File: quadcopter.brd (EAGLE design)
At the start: 130 x 130 mm, 66 parts, among them J1 ISP, J4 SIP-10_TH-254X10, M1 MOTOR_PADS, M2 MOTOR_PADS, M3 MOTOR_PADS, M4 MOTOR_PADS, U1 ATMEGA128RFA1, Y1 16MHz

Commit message: Version before generating cam
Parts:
- LED2, LED3: value BLUE -> green; device Yueqi Wang-Lab2:LED5MM -> quadparts_prebuilt:LEDSC125X200X120-2_HS
- moved LED4 73.5 mm to (31.0, -3.00), turned to 0 degrees
- moved LED1 73.5 mm to (31.0, 3.00), turned to 0 degrees
- moved C16 68.3 mm to (6.74, 37.6), turned to 270 degrees
- moved R15 48.0 mm to (-19.1, -15.2), turned to 270 degrees
- moved U$7 46.2 mm to (-7.45, -21.6), turned to 0 degrees
- moved C19 35.8 mm to (22.6, -16.8), turned to 270 degrees
- moved C24 35.1 mm to (-6.99, 4.57)
- moved U$2 33.2 mm to (17.0, -22.0), turned to 270 degrees
- moved C23 26.2 mm to (8.12, 4.38), turned to 180 degrees
- moved BATT1 24.8 mm to (0.00, 0.00), turned to 180 degrees
- moved C18 22.1 mm to (11.8, -16.2), turned to 90 degrees
- moved J2 22.0 mm to (1.28, -22.2), turned to 270 degrees
- moved C22 20.1 mm to (8.15, 7.99), turned to 180 degrees
- moved C20 15.7 mm to (0.83, 7.28), turned to 90 degrees
- moved MOFSET4 15.4 mm to (30.5, -26.6)
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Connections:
- net GND: now also LED2.C, LED3.C; no longer LED2.K, LED3.K
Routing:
- net DTR: track 86.9 -> 8.24 mm, vias 2 -> 0
- net VBAT: track 127.0 -> 84.4 mm, vias 4 -> 6
- net BAT_GND: track 234.5 -> 275.4 mm, vias 2 -> 0
- net PG1: track 22.1 -> 60.4 mm, vias 0 -> 2
- net SCK: track 21.9 -> 59.8 mm
- net PG0: track 27.1 -> 64.2 mm
- net RX0: track 47.8 -> 82.5 mm
- net RESET: track 102.6 -> 68.2 mm, vias 2 -> 1
- net MOSI: track 27.9 -> 62.1 mm
- net GND: track 266.6 -> 297.4 mm, vias 45 -> 41
- net PE3: track 124.3 -> 99.1 mm
- net SDA: track 114.8 -> 89.9 mm, vias 5 -> 2
- net TX0: track 47.7 -> 62.7 mm
- net FILTERED_1: track 19.8 -> 34.3 mm, vias 0 -> 2
- net PB5: track 111.1 -> 97.4 mm, vias 0 -> 1
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- added copper zone on layer 1, net GND
- added copper zone on layer 2, net GND
- added copper zone on layer 2, net N$3
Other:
- board text added: "CTS"
- board text added: "DTR"
- board text added: "RXI"
- board text added: "TXO"

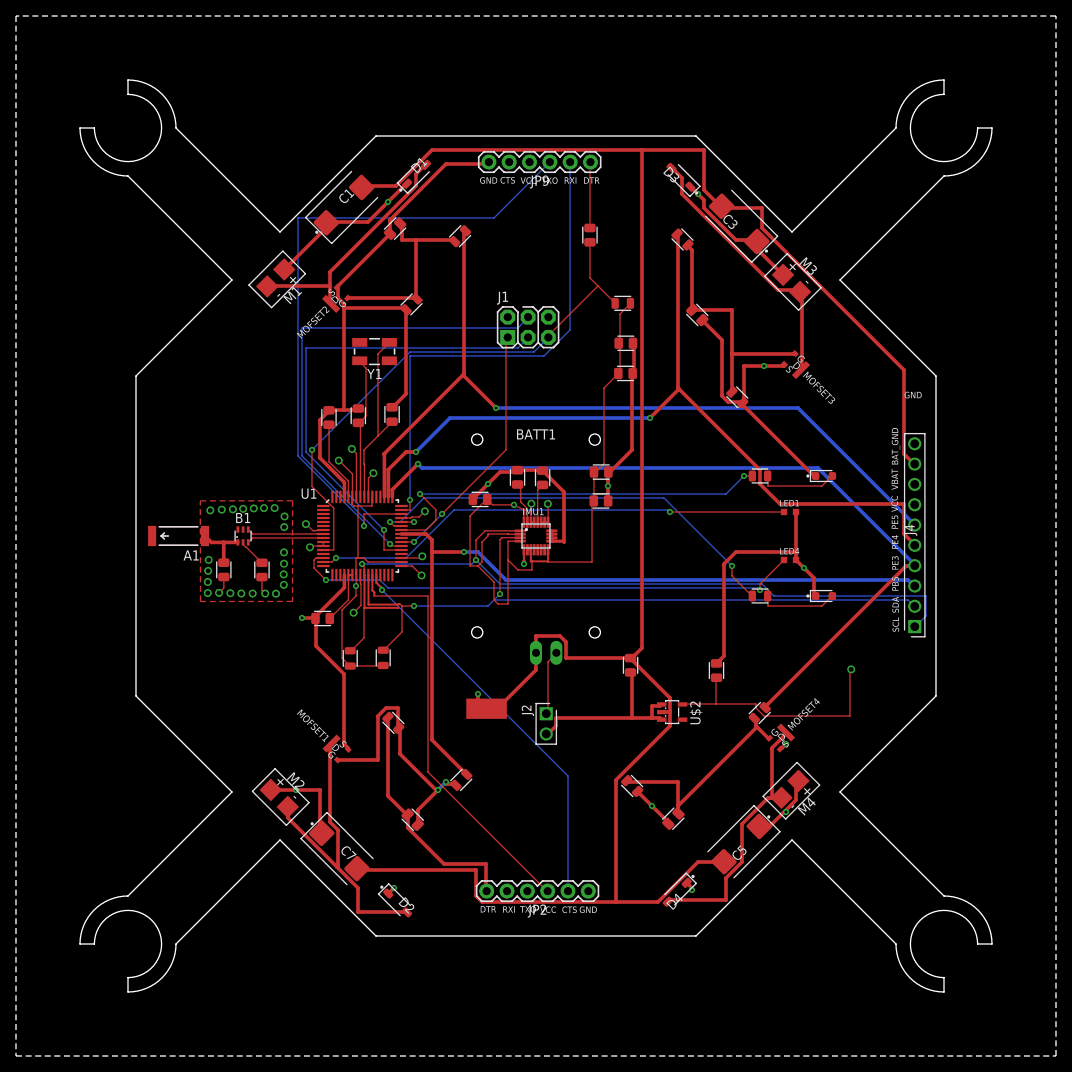
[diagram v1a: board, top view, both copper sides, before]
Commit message: Version May 8th 11pm
Version before rerun the autorouter with new dru
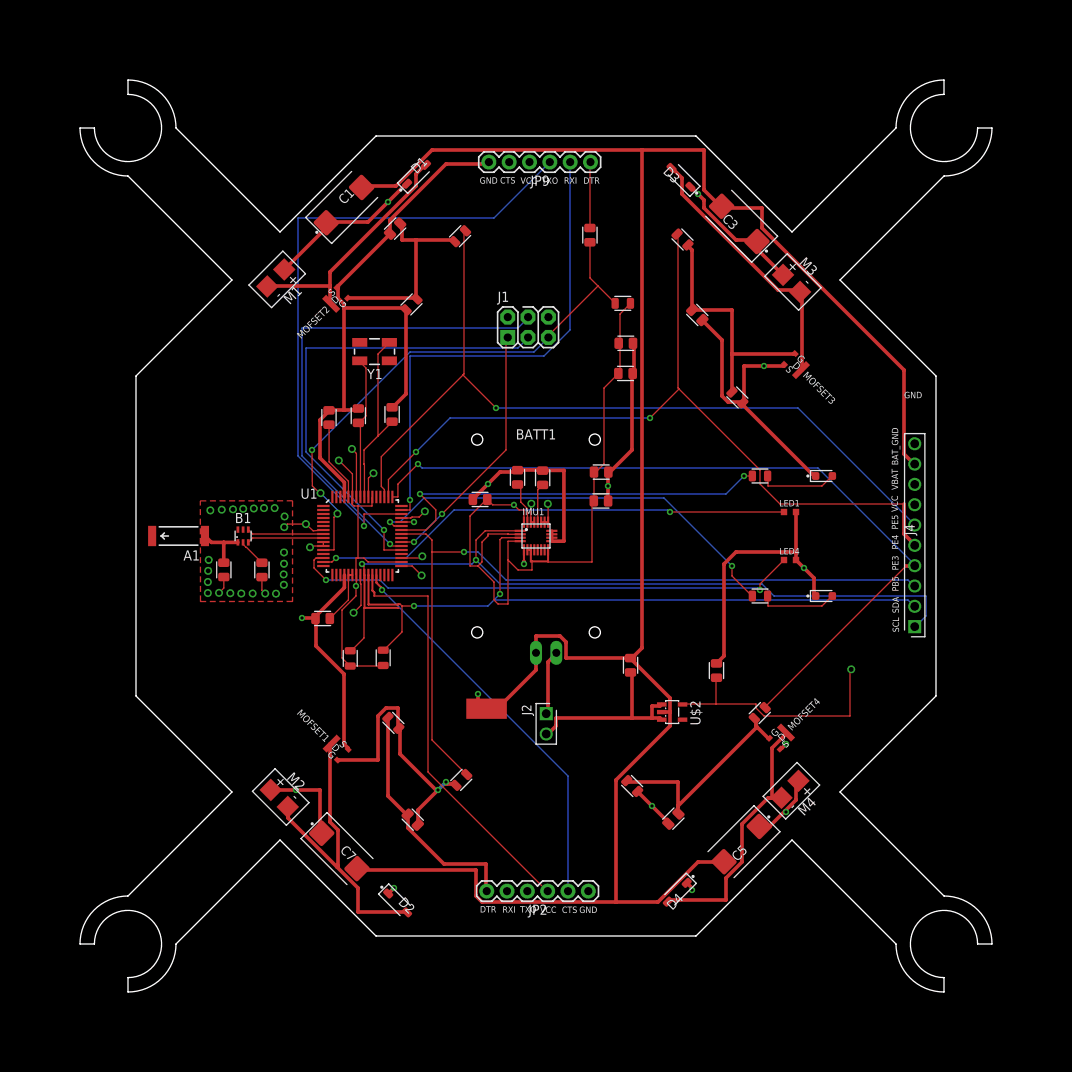
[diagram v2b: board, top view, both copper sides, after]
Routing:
- net GND: track 297.4 -> 301.6 mm
- net PE4: track 104.3 -> 103.4 mm
- net RESET: track 68.2 -> 68.7 mm, vias 1 -> 3
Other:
- board size 130 x 130 mm -> 114 x 114 mm

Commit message: Board and Schematic that pass DFM
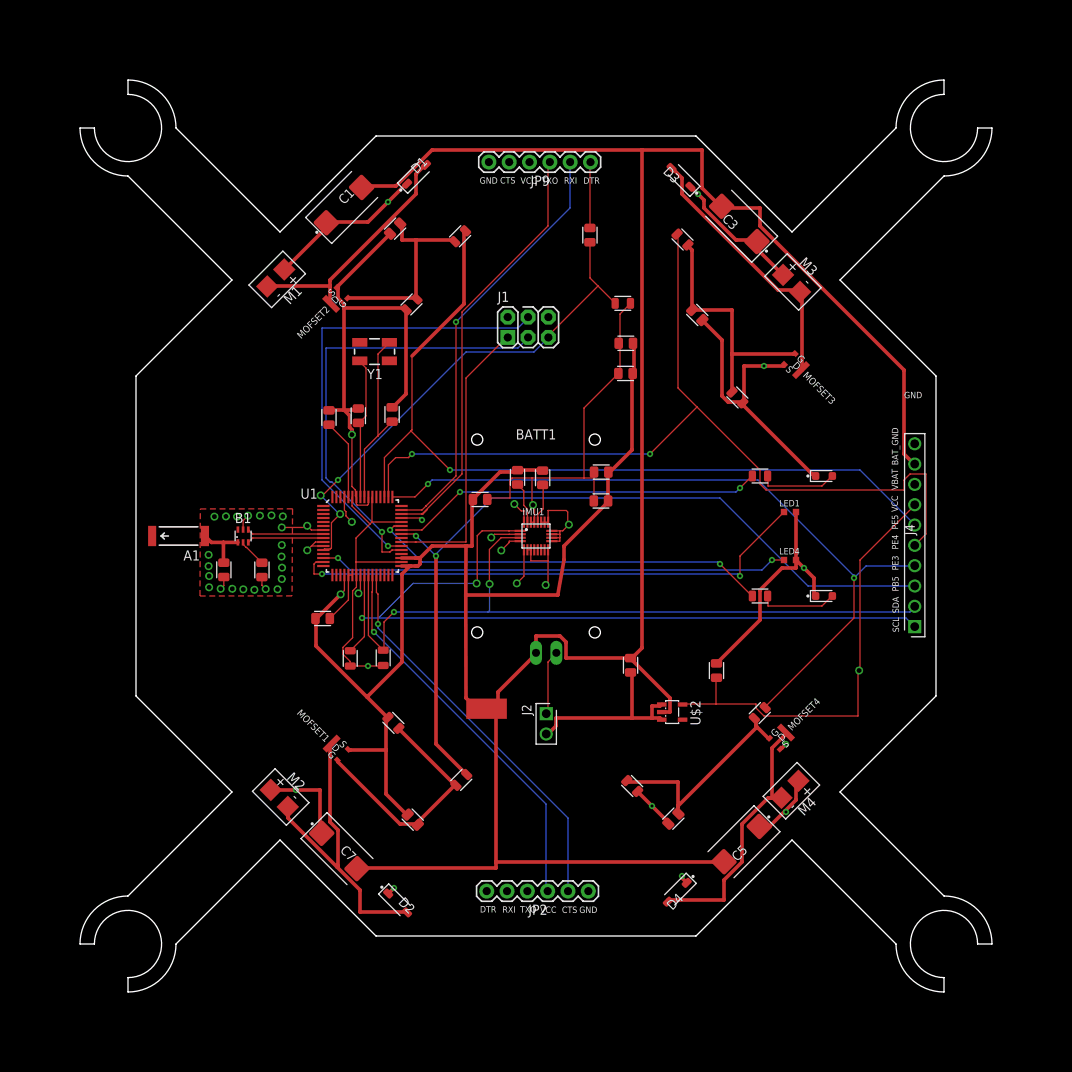
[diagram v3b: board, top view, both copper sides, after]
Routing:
- net GND: track 301.6 -> 335.2 mm, vias 41 -> 35
- net RX0: track 82.5 -> 54.0 mm, vias 1 -> 0
- net BAT_GND: track 275.4 -> 262.8 mm
- net VCC: track 174.9 -> 164.5 mm, vias 6 -> 7
- net PE4: track 103.4 -> 113.2 mm
- net TX0: track 62.7 -> 53.8 mm
- net PE3: track 99.3 -> 92.8 mm, vias 1 -> 2
- net PG1: track 60.4 -> 66.2 mm
- net PG0: track 64.2 -> 58.7 mm
- net RESET: track 68.7 -> 63.8 mm
- net PB6: track 51.4 -> 46.7 mm
- net PB5: track 97.3 -> 101.9 mm, vias 1 -> 2
- net SCL: track 101.6 -> 105.7 mm
- net N$5: track 52.6 -> 48.7 mm, vias 0 -> 1
- net MISO: track 32.1 -> 35.9 mm, vias 2 -> 0
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
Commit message: New board passed DFM with new DRU and CAM
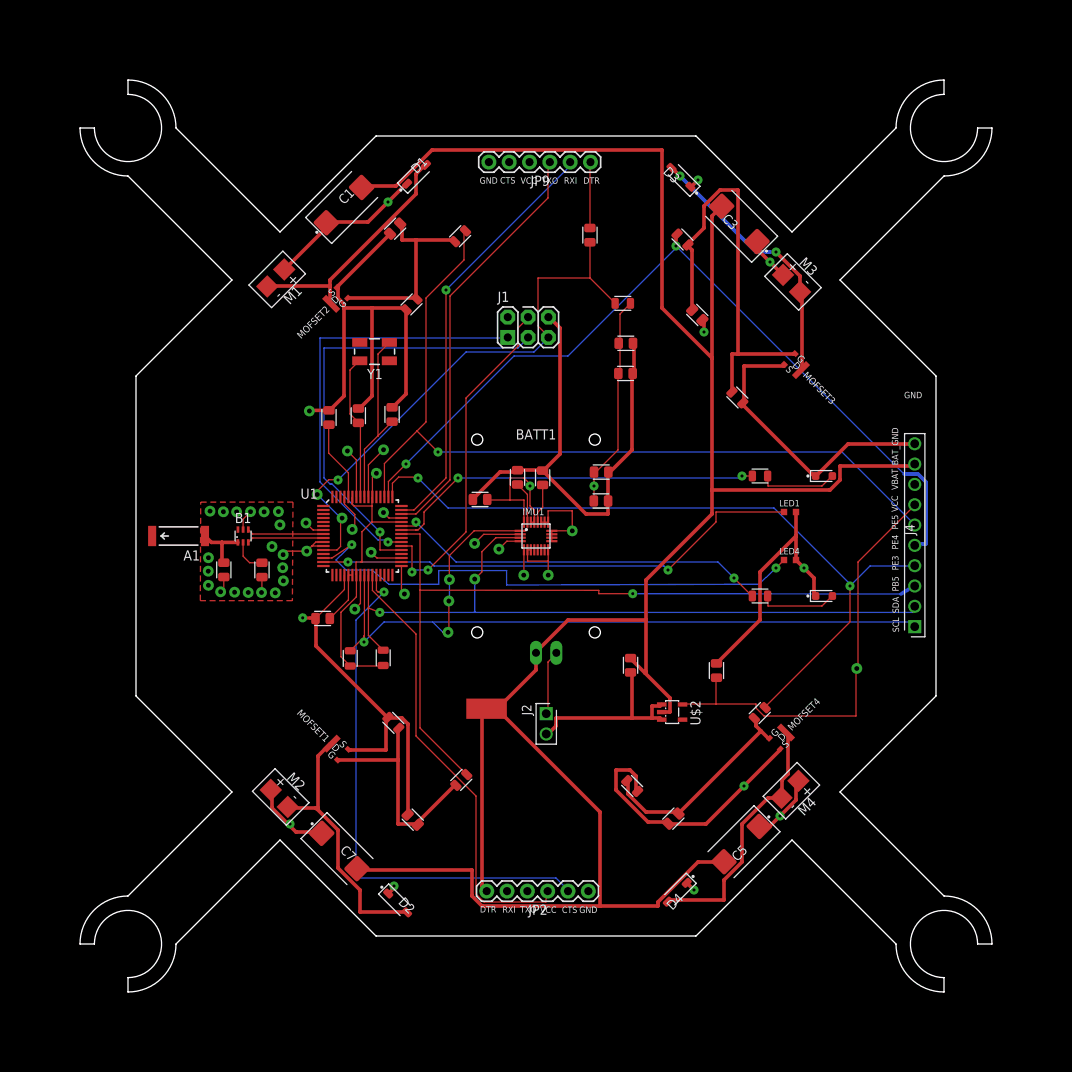
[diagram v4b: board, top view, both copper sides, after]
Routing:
- net GND: track 335.2 -> 366.0 mm
- net FILTERED_3: track 31.5 -> 52.3 mm
- net MISO: track 35.9 -> 54.8 mm, vias 0 -> 1
- net N$4: track 49.4 -> 67.4 mm
- net MOSI: track 58.7 -> 43.5 mm, vias 1 -> 2
- net BAT_GND: track 262.8 -> 274.9 mm
- net VBAT: track 84.3 -> 72.5 mm, vias 6 -> 7
- net PG0: track 58.7 -> 68.7 mm
- net PE4: track 113.2 -> 104.4 mm
- net N$5: track 48.7 -> 55.9 mm, vias 1 -> 0
- net RESET: track 63.8 -> 71.0 mm
- net FLYBACK_1: track 38.8 -> 33.8 mm
- net PB5: track 101.9 -> 97.3 mm, vias 2 -> 1
- net PG1: track 66.2 -> 61.7 mm
- net VCC: track 164.5 -> 160.7 mm
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
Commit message: New board  after Prof. review on May 10th
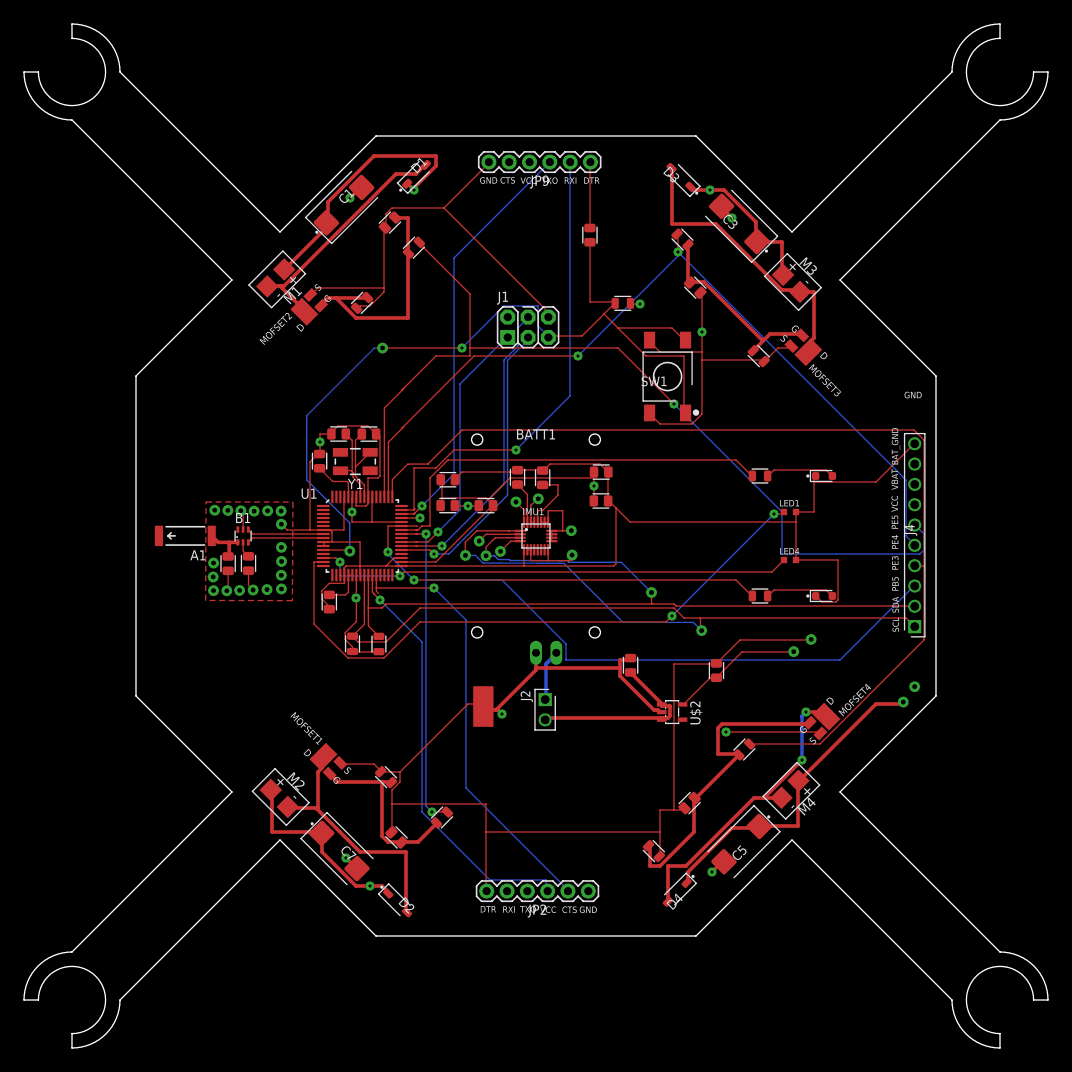
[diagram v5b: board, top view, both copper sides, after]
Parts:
- added SW1: PUSHBUTTON_SMD-VERTICAL-1, quadparts_prebuilt:TE_FSM8JSMA_HS
- moved C11 28.0 mm to (-11.0, 7.03)
- moved C12 27.7 mm to (-11.0, 3.81)
- moved Y1 14.0 mm to (-22.6, 9.31)
- moved R8 8.58 mm to (14.7, -39.4)
- moved R4 6.84 mm to (-18.7, -30.1)
- moved R2 6.19 mm to (-21.7, 29.1)
- moved R1 5.95 mm to (-15.3, 36.0)
- moved R6 5.81 mm to (27.8, 22.5)
- moved C9 5.58 mm to (-27.1, 9.36)
- moved MOFSET4 5.39 mm to (35.6, -24.7)
- moved R3 5.28 mm to (-11.8, -35.2)
- moved R7 4.95 mm to (26.0, -26.7)
- moved C14 3.79 mm to (-20.9, 12.7), turned to 0 degrees
- moved MOFSET2 3.44 mm to (-28.2, 30.1)
- moved C4 3.42 mm to (19.9, 31.0)
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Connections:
- net GND: now also SW1.3, SW1.4
- net RESET: now also SW1.1, SW1.2
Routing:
- net BAT_GND: track 274.9 -> 41.1 mm, vias 0 -> 6
- net GND: track 366.0 -> 456.6 mm, vias 35 -> 25
- net VBAT: track 72.5 -> 142.2 mm, vias 7 -> 4
- net VCC: track 160.7 -> 119.2 mm, vias 7 -> 10
- net RESET: track 71.0 -> 110.8 mm
- net PE3: track 93.7 -> 125.1 mm, vias 2 -> 0
- net FILTERED_3: track 52.3 -> 24.3 mm
- net SCL: track 103.4 -> 125.7 mm, vias 4 -> 2
- net MISO: track 54.8 -> 33.1 mm
- net SCK: track 57.1 -> 37.3 mm
- net PG1: track 61.7 -> 77.0 mm
- net SDA: track 92.8 -> 106.8 mm
- net PB5: track 97.3 -> 110.3 mm, vias 1 -> 2
- net N$4: track 67.4 -> 54.5 mm
- net FILTERED_4: track 27.1 -> 39.6 mm
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- added copper zone on layer 15, net BAT_GND
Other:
- board size 114 x 114 mm -> 128 x 128 mm
